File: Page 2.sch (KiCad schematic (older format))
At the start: 24 parts

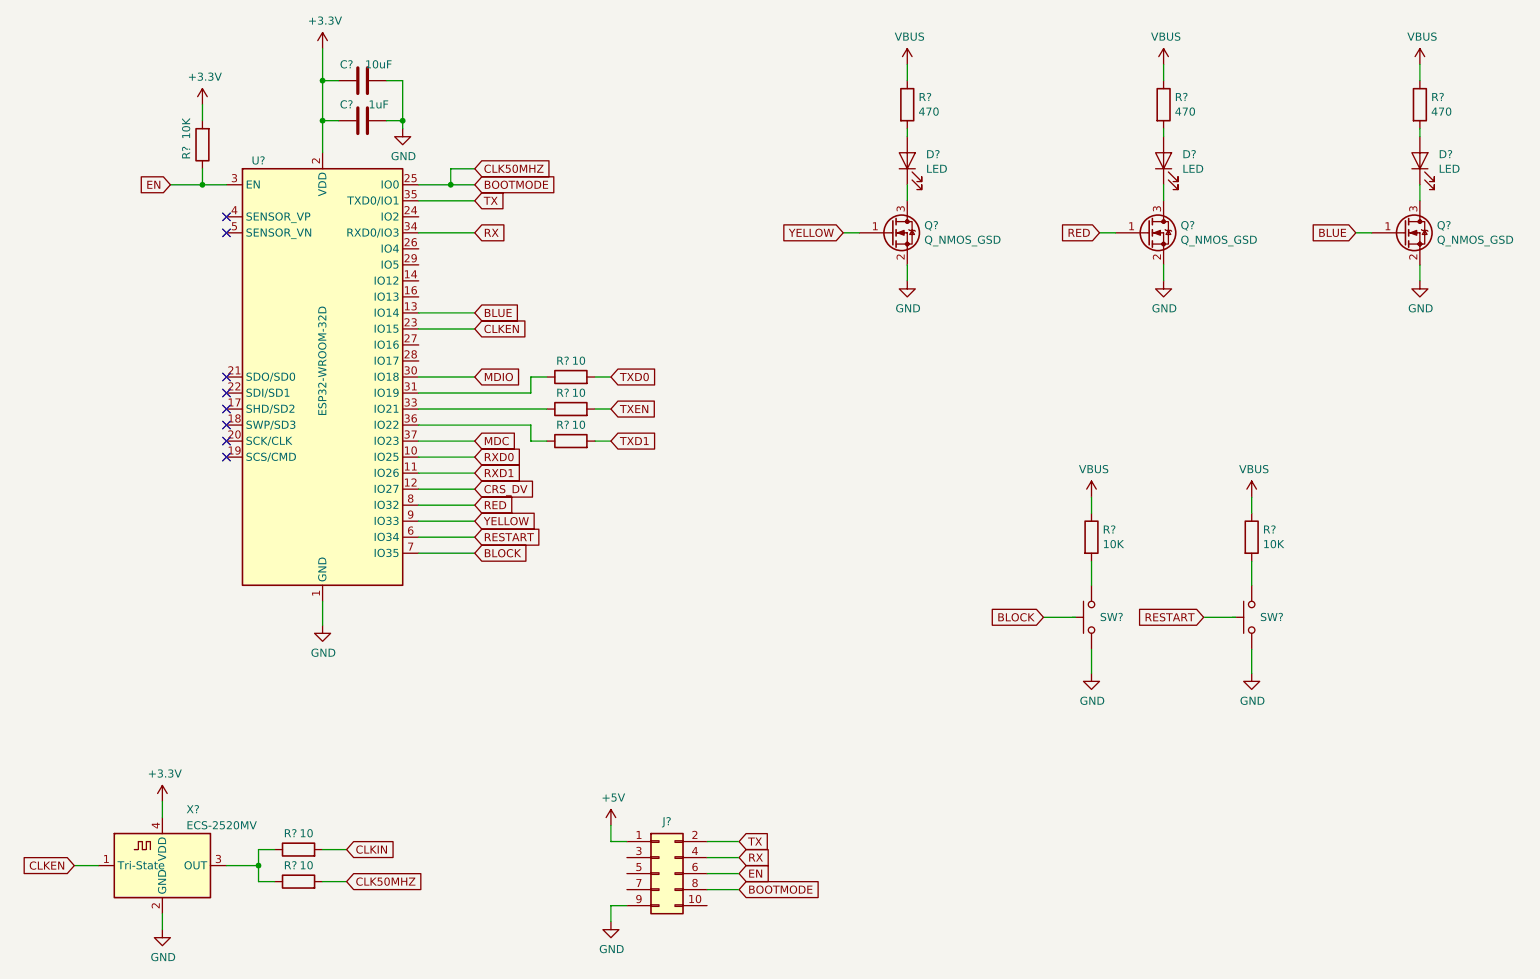
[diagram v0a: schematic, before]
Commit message: Corrected mistakes, added refdes
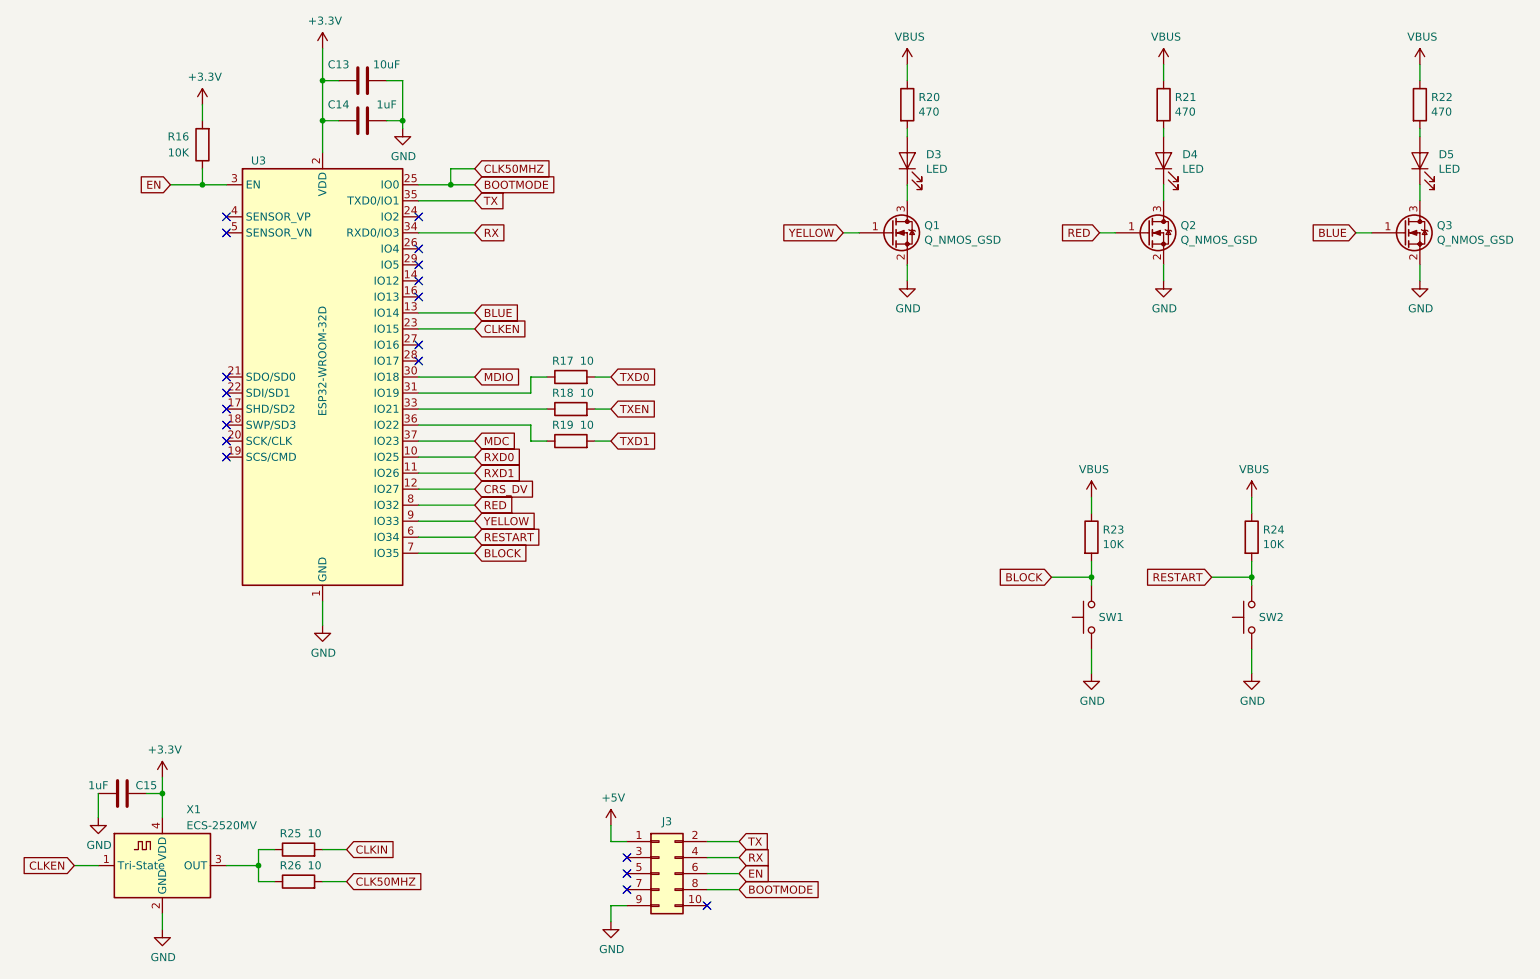
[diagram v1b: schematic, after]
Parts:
- added C15: 1uF, symbol Device:C
- gave numbers to parts that had none: 24
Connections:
- net +3V3: now also C15.2
- net BLOCK: now also R23.2, SW1.2
- net GND: now also C15.1
- net RESTART: now also R24.2, SW2.2
- no-connect marks 8 -> 19

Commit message: Started assigning footprints
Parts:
- C13, C14, C15: footprint (none) -> Capacitor_SMD:C_0603_1608Metric
- D3, D4, D5: footprint (none) -> Diode_SMD:D_0603_1608Metric
- R16, R17, R18, R19, R20, R21, R22, R23, R24, R25, R26: footprint (none) -> Resistor_SMD:R_0603_1608Metric
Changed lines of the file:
@@
 F 0 "R18" V 4550 3750 50  0000 C CNN
 F 1 "10" V 4550 3600 50  0000 C CNN
-F 2 "" V 4380 3700 50  0001 C CNN
+F 2 "Resistor_SMD:R_0603_1608Metric" V 4380 3700 50  0001 C CNN
 F 3 "~" H 4450 3700 50  0001 C CNN
 	1    4450 3700
@@
 F 0 "R19" V 4550 3950 50  0000 C CNN
 F 1 "10" V 4550 3800 50  0000 C CNN
-F 2 "" V 4380 3900 50  0001 C CNN
+F 2 "Resistor_SMD:R_0603_1608Metric" V 4380 3900 50  0001 C CNN
 F 3 "~" H 4450 3900 50  0001 C CNN
 	1    4450 3900
@@
 F 0 "C14" V 3050 1750 50  0000 C CNN
 F 1 "1uF" V 3050 2050 50  0000 C CNN
-F 2 "" H 3188 1750 50  0001 C CNN
+F 2 "Capacitor_SMD:C_0603_1608Metric" H 3188 1750 50  0001 C CNN
 F 3 "~" H 3150 1900 50  0001 C CNN
 	1    3150 1900
@@
 F 0 "C13" V 3050 1500 50  0000 C CNN
 F 1 "10uF" V 3050 1800 50  0000 C CNN
-F 2 "" H 3188 1500 50  0001 C CNN
+F 2 "Capacitor_SMD:C_0603_1608Metric" H 3188 1500 50  0001 C CNN
 F 3 "~" H 3150 1650 50  0001 C CNN
 	1    3150 1650
@@
 F 0 "R16" H 2300 2000 50  0000 C CNN
 F 1 "10K" H 2300 2100 50  0000 C CNN
-F 2 "" V 2080 2050 50  0001 C CNN
+F 2 "Resistor_SMD:R_0603_1608Metric" V 2080 2050 50  0001 C CNN
 F 3 "~" H 2150 2050 50  0001 C CNN
 	1    2150 2050
@@
 F 0 "R17" V 4550 3550 50  0000 C CNN
 F 1 "10" V 4550 3400 50  0000 C CNN
-F 2 "" V 4380 3500 50  0001 C CNN
+F 2 "Resistor_SMD:R_0603_1608Metric" V 4380 3500 50  0001 C CNN
 F 3 "~" H 4450 3500 50  0001 C CNN
 	1    4450 3500
@@
 F 0 "R22" H 9820 1846 50  0000 L CNN
 F 1 "470" H 9820 1755 50  0000 L CNN
-F 2 "" V 9680 1800 50  0001 C CNN
+F 2 "Resistor_SMD:R_0603_1608Metric" V 9680 1800 50  0001 C CNN
 F 3 "~" H 9750 1800 50  0001 C CNN
 	1    9750 1800
@@
 F 0 "D5" V 9789 2033 50  0000 R CNN
 F 1 "LED" V 9698 2033 50  0000 R CNN
-F 2 "" H 9750 2150 50  0001 C CNN
+F 2 "Diode_SMD:D_0603_1608Metric" H 9750 2150 50  0001 C CNN
 F 3 "~" H 9750 2150 50  0001 C CNN
 	1    9750 2150
@@
 F 0 "R21" H 8220 1846 50  0000 L CNN
 F 1 "470" H 8220 1755 50  0000 L CNN
-F 2 "" V 8080 1800 50  0001 C CNN
+F 2 "Resistor_SMD:R_0603_1608Metric" V 8080 1800 50  0001 C CNN
 F 3 "~" H 8150 1800 50  0001 C CNN
 	1    8150 1800
@@
 F 0 "D4" V 8189 2033 50  0000 R CNN
 F 1 "LED" V 8098 2033 50  0000 R CNN
-F 2 "" H 8150 2150 50  0001 C CNN
+F 2 "Diode_SMD:D_0603_1608Metric" H 8150 2150 50  0001 C CNN
 F 3 "~" H 8150 2150 50  0001 C CNN
 	1    8150 2150
@@
 F 0 "R20" H 6620 1846 50  0000 L CNN
 F 1 "470" H 6620 1755 50  0000 L CNN
-F 2 "" V 6480 1800 50  0001 C CNN
+F 2 "Resistor_SMD:R_0603_1608Metric" V 6480 1800 50  0001 C CNN
 F 3 "~" H 6550 1800 50  0001 C CNN
 	1    6550 1800
@@
 F 0 "D3" V 6589 2033 50  0000 R CNN
 F 1 "LED" V 6498 2033 50  0000 R CNN
-F 2 "" H 6550 2150 50  0001 C CNN
+F 2 "Diode_SMD:D_0603_1608Metric" H 6550 2150 50  0001 C CNN
 F 3 "~" H 6550 2150 50  0001 C CNN
 	1    6550 2150
@@
 F 0 "R25" V 2850 6500 50  0000 C CNN
 F 1 "10" V 2850 6350 50  0000 C CNN
-F 2 "" V 2680 6450 50  0001 C CNN
+F 2 "Resistor_SMD:R_0603_1608Metric" V 2680 6450 50  0001 C CNN
 F 3 "~" H 2750 6450 50  0001 C CNN
 	1    2750 6450
@@
 F 0 "R26" V 2850 6700 50  0000 C CNN
 F 1 "10" V 2850 6550 50  0000 C CNN
-F 2 "" V 2680 6650 50  0001 C CNN
+F 2 "Resistor_SMD:R_0603_1608Metric" V 2680 6650 50  0001 C CNN
 F 3 "~" H 2750 6650 50  0001 C CNN
 	1    2750 6650
@@
 F 0 "R23" H 7770 4546 50  0000 L CNN
 F 1 "10K" H 7770 4455 50  0000 L CNN
-F 2 "" V 7630 4500 50  0001 C CNN
+F 2 "Resistor_SMD:R_0603_1608Metric" V 7630 4500 50  0001 C CNN
 F 3 "~" H 7700 4500 50  0001 C CNN
 	1    7700 4500
@@
 F 0 "R24" H 8770 4546 50  0000 L CNN
 F 1 "10K" H 8770 4455 50  0000 L CNN
-F 2 "" V 8630 4500 50  0001 C CNN
+F 2 "Resistor_SMD:R_0603_1608Metric" V 8630 4500 50  0001 C CNN
 F 3 "~" H 8700 4500 50  0001 C CNN
 	1    8700 4500
@@
 F 0 "C15" V 1700 5950 50  0000 C CNN
 F 1 "1uF" V 1700 6250 50  0000 C CNN
-F 2 "" H 1688 5950 50  0001 C CNN
+F 2 "Capacitor_SMD:C_0603_1608Metric" H 1688 5950 50  0001 C CNN
 F 3 "~" H 1650 6100 50  0001 C CNN
 	1    1650 6100

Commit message: Assigning footprints
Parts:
- J3: footprint (none) -> Connector_PinSocket_2.54mm:PinSocket_2x05_P2.54mm_Vertical
- Q1, Q2, Q3: footprint (none) -> digikey-footprints:SOT-23-3
- SW1, SW2: footprint (none) -> kicad-library:222CMVBAR
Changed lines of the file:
@@
 EESchema Schematic File Version 4
-LIBS:EsperDNS-cache
 EELAYER 30 0
 EELAYER END
@@
 F 0 "Q3" H 9856 2646 50  0000 L CNN
 F 1 "Q_NMOS_GSD" H 9856 2555 50  0000 L CNN
-F 2 "" H 9850 2700 50  0001 C CNN
+F 2 "digikey-footprints:SOT-23-3" H 9850 2700 50  0001 C CNN
 F 3 "~" H 9650 2600 50  0001 C CNN
 	1    9650 2600
@@
 F 0 "Q2" H 8256 2646 50  0000 L CNN
 F 1 "Q_NMOS_GSD" H 8256 2555 50  0000 L CNN
-F 2 "" H 8250 2700 50  0001 C CNN
+F 2 "digikey-footprints:SOT-23-3" H 8250 2700 50  0001 C CNN
 F 3 "~" H 8050 2600 50  0001 C CNN
 	1    8050 2600
@@
 F 0 "Q1" H 6656 2646 50  0000 L CNN
 F 1 "Q_NMOS_GSD" H 6656 2555 50  0000 L CNN
-F 2 "" H 6650 2700 50  0001 C CNN
+F 2 "digikey-footprints:SOT-23-3" H 6650 2700 50  0001 C CNN
 F 3 "~" H 6450 2600 50  0001 C CNN
 	1    6450 2600
@@
 F 0 "SW1" V 7700 4800 50  0000 L CNN
 F 1 "SW_Push" V 7700 4550 50  0001 L CNN
-F 2 "" H 7700 5200 50  0001 C CNN
+F 2 "kicad-library:222CMVBAR" H 7700 5200 50  0001 C CNN
 F 3 "~" H 7700 5200 50  0001 C CNN
 	1    7700 5000
@@
 F 0 "SW2" V 8700 4800 50  0000 L CNN
 F 1 "SW_Push" V 8700 4550 50  0001 L CNN
-F 2 "" H 8700 5200 50  0001 C CNN
+F 2 "kicad-library:222CMVBAR" H 8700 5200 50  0001 C CNN
 F 3 "~" H 8700 5200 50  0001 C CNN
 	1    8700 5000
@@
 F 0 "J3" H 5050 6925 50  0000 C CNN
 F 1 "Conn_02x05_Odd_Even" H 5050 6926 50  0001 C CNN
-F 2 "" H 5000 6600 50  0001 C CNN
+F 2 "Connector_PinSocket_2.54mm:PinSocket_2x05_P2.54mm_Vertical" H 5000 6600 50  0001 C CNN
 F 3 "~" H 5000 6600 50  0001 C CNN
 	1    5000 6600

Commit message: Started laying out board
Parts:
- removed SW1, SW2: SW_Push, kicad-library:222CMVBAR, symbol Switch:SW_Push
- added SW1, SW2: 222CMVBAR, My Footprints:222CMVBAR, symbol My_Symbols:222CMVBAR
- C15: value 1uF -> 0.1uF
- U3: symbol RF_Module:ESP32-WROOM-32D -> EsperDNS-rescue:ESP32-WROOM-32D-RF_Module
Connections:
- net BLOCK: now also SW1.3, SW1.4
- net GND: now also SW1.1, SW1.2, SW2.1, SW2.2
- net RESTART: now also SW2.3, SW2.4
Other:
- moved on the sheet: C15
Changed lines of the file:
@@
 EESchema Schematic File Version 4
+LIBS:EsperDNS-cache
 EELAYER 30 0
 EELAYER END
@@
 $EndComp
 $Comp
-L RF_Module:ESP32-WROOM-32D U3
+L EsperDNS-rescue:ESP32-WROOM-32D-RF_Module U3
 U 1 1 5DF25F0A
 P 2900 3500
+AR Path="/5DF25F0A" Ref="U3"  Part="1"
+AR Path="/5DED3446/5DF25F0A" Ref="U3"  Part="1"
 F 0 "U3" H 2500 4850 50  0000 C CNN
 F 1 "ESP32-WROOM-32D" V 2900 3600 50  0000 C CNN
@@
 	1500 6550 1350 6550
 $Comp
-L Switch:SW_Push SW1
-U 1 1 5DF938CA
-P 7700 5000
-F 0 "SW1" V 7700 4800 50  0000 L CNN
-F 1 "SW_Push" V 7700 4550 50  0001 L CNN
-F 2 "kicad-library:222CMVBAR" H 7700 5200 50  0001 C CNN
-F 3 "~" H 7700 5200 50  0001 C CNN
-	1    7700 5000
-	0    -1   -1   0
-$EndComp
-$Comp
 L power:VBUS #PWR?
 U 1 1 5DF9568B
@@
 	7700 4650 7700 4750
 Wire Wire Line
-	7700 5350 7700 5200
+	7700 5350 7700 5250
 Text GLabel 7450 4750 0    50   Input ~ 0
 BLOCK
-$Comp
-L Switch:SW_Push SW2
-U 1 1 5DFA637D
-P 8700 5000
-F 0 "SW2" V 8700 4800 50  0000 L CNN
-F 1 "SW_Push" V 8700 4550 50  0001 L CNN
-F 2 "kicad-library:222CMVBAR" H 8700 5200 50  0001 C CNN
-F 3 "~" H 8700 5200 50  0001 C CNN
-	1    8700 5000
-	0    -1   -1   0
-$EndComp
 $Comp
 L power:VBUS #PWR?
@@
 	8700 4650 8700 4750
 Wire Wire Line
-	8700 5350 8700 5200
+	8700 5350 8700 5250
 Text GLabel 8450 4750 0    50   Input ~ 0
 RESTART
@@
 NoConn ~ 4800 6600
 NoConn ~ 4800 6500
-$Comp
-L Device:C C15
-U 1 1 5E07AF59
-P 1650 6100
-F 0 "C15" V 1700 5950 50  0000 C CNN
-F 1 "1uF" V 1700 6250 50  0000 C CNN
-F 2 "Capacitor_SMD:C_0603_1608Metric" H 1688 5950 50  0001 C CNN
-F 3 "~" H 1650 6100 50  0001 C CNN
-	1    1650 6100
-	0    -1   -1   0
-$EndComp
-Wire Wire Line
-	1800 6100 1900 6100
+Wire Wire Line
+	1750 6100 1900 6100
 Wire Wire Line
 	1900 6250 1900 6100
@@
 L power:GND #PWR0148
 U 1 1 5E082755
-P 1500 6250
-F 0 "#PWR0148" H 1500 6000 50  0001 C CNN
-F 1 "GND" H 1505 6077 50  0000 C CNN
-F 2 "" H 1500 6250 50  0001 C CNN
-F 3 "" H 1500 6250 50  0001 C CNN
-	1    1500 6250
-	1    0    0    -1
-$EndComp
-Wire Wire Line
-	1500 6100 1500 6250
+P 1400 6200
+F 0 "#PWR0148" H 1400 5950 50  0001 C CNN
+F 1 "GND" H 1405 6027 50  0000 C CNN
+F 2 "" H 1400 6200 50  0001 C CNN
+F 3 "" H 1400 6200 50  0001 C CNN
+	1    1400 6200
+	1    0    0    -1
+$EndComp
 NoConn ~ 3500 2500
 NoConn ~ 3500 2700
@@
 Wire Wire Line
 	8700 4750 8700 4800
+$Comp
+L Device:C C15
+U 1 1 5E07AF59
+P 1600 6100
+F 0 "C15" V 1650 5950 50  0000 C CNN
+F 1 "0.1uF" V 1650 6250 50  0000 C CNN
+F 2 "Capacitor_SMD:C_0603_1608Metric" H 1638 5950 50  0001 C CNN
+F 3 "~" H 1600 6100 50  0001 C CNN
+	1    1600 6100
+	0    -1   -1   0
+$EndComp
+Wire Wire Line
+	1450 6100 1400 6100
+Wire Wire Line
+	1400 6100 1400 6200
+$Comp
+L My_Symbols:222CMVBAR SW1
+U 1 1 5DFB5FF6
+P 7700 5000
+F 0 "SW1" V 7700 4952 50  0000 R CNN
+F 1 "222CMVBAR" V 7655 4952 50  0001 R CNN
+F 2 "My Footprints:222CMVBAR" H 7700 5200 50  0001 C CNN
+F 3 "~" H 7700 5200 50  0001 C CNN
+	1    7700 5000
+	0    -1   -1   0
+$EndComp
+$Comp
+L My_Symbols:222CMVBAR SW2
+U 1 1 5DFB7206
+P 8700 5000
+F 0 "SW2" V 8700 4952 50  0000 R CNN
+F 1 "222CMVBAR" V 8655 4952 50  0001 R CNN
+F 2 "My Footprints:222CMVBAR" H 8700 5200 50  0001 C CNN
+F 3 "~" H 8700 5200 50  0001 C CNN
+	1    8700 5000
+	0    -1   -1   0
+$EndComp
+Wire Wire Line
+	7750 5200 7750 5250
+Wire Wire Line
+	7750 5250 7700 5250
+Connection ~ 7700 5250
+Wire Wire Line
+	7700 5250 7700 5200
+Wire Wire Line
+	7750 4800 7750 4750
+Wire Wire Line
+	7750 4750 7700 4750
+Wire Wire Line
+	8750 4800 8750 4750
+Wire Wire Line
+	8750 4750 8700 4750
+Wire Wire Line
+	8750 5200 8750 5250
+Wire Wire Line
+	8750 5250 8700 5250
+Connection ~ 8700 5250
+Wire Wire Line
+	8700 5250 8700 5200
 $EndSCHEMATC

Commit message: Stuff
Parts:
- R25, R26: value 10 -> 33
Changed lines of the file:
@@
 Wire Wire Line
 	4700 3500 4600 3500
-Text GLabel 3850 3200 2    50   Input ~ 0
-CLKEN
 Wire Wire Line
 	3500 3200 3850 3200
@@
 P 2750 6450
 F 0 "R25" V 2850 6500 50  0000 C CNN
-F 1 "10" V 2850 6350 50  0000 C CNN
+F 1 "33" V 2850 6350 50  0000 C CNN
 F 2 "Resistor_SMD:R_0603_1608Metric" V 2680 6450 50  0001 C CNN
 F 3 "~" H 2750 6450 50  0001 C CNN
@@
 P 2750 6650
 F 0 "R26" V 2850 6700 50  0000 C CNN
-F 1 "10" V 2850 6550 50  0000 C CNN
+F 1 "33" V 2850 6550 50  0000 C CNN
 F 2 "Resistor_SMD:R_0603_1608Metric" V 2680 6650 50  0001 C CNN
 F 3 "~" H 2750 6650 50  0001 C CNN
@@
 Wire Wire Line
 	1900 6950 1900 6850
-Text GLabel 1350 6550 0    50   Input ~ 0
-CLKEN
 Wire Wire Line
 	1500 6550 1350 6550
@@
 	1    0    0    -1
 $EndComp
+Text GLabel 1350 6550 0    50   Input ~ 0
+CLKEN
+Text GLabel 3850 3200 2    50   Input ~ 0
+CLKEN
 $EndSCHEMATC
